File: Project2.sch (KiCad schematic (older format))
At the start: 4 parts

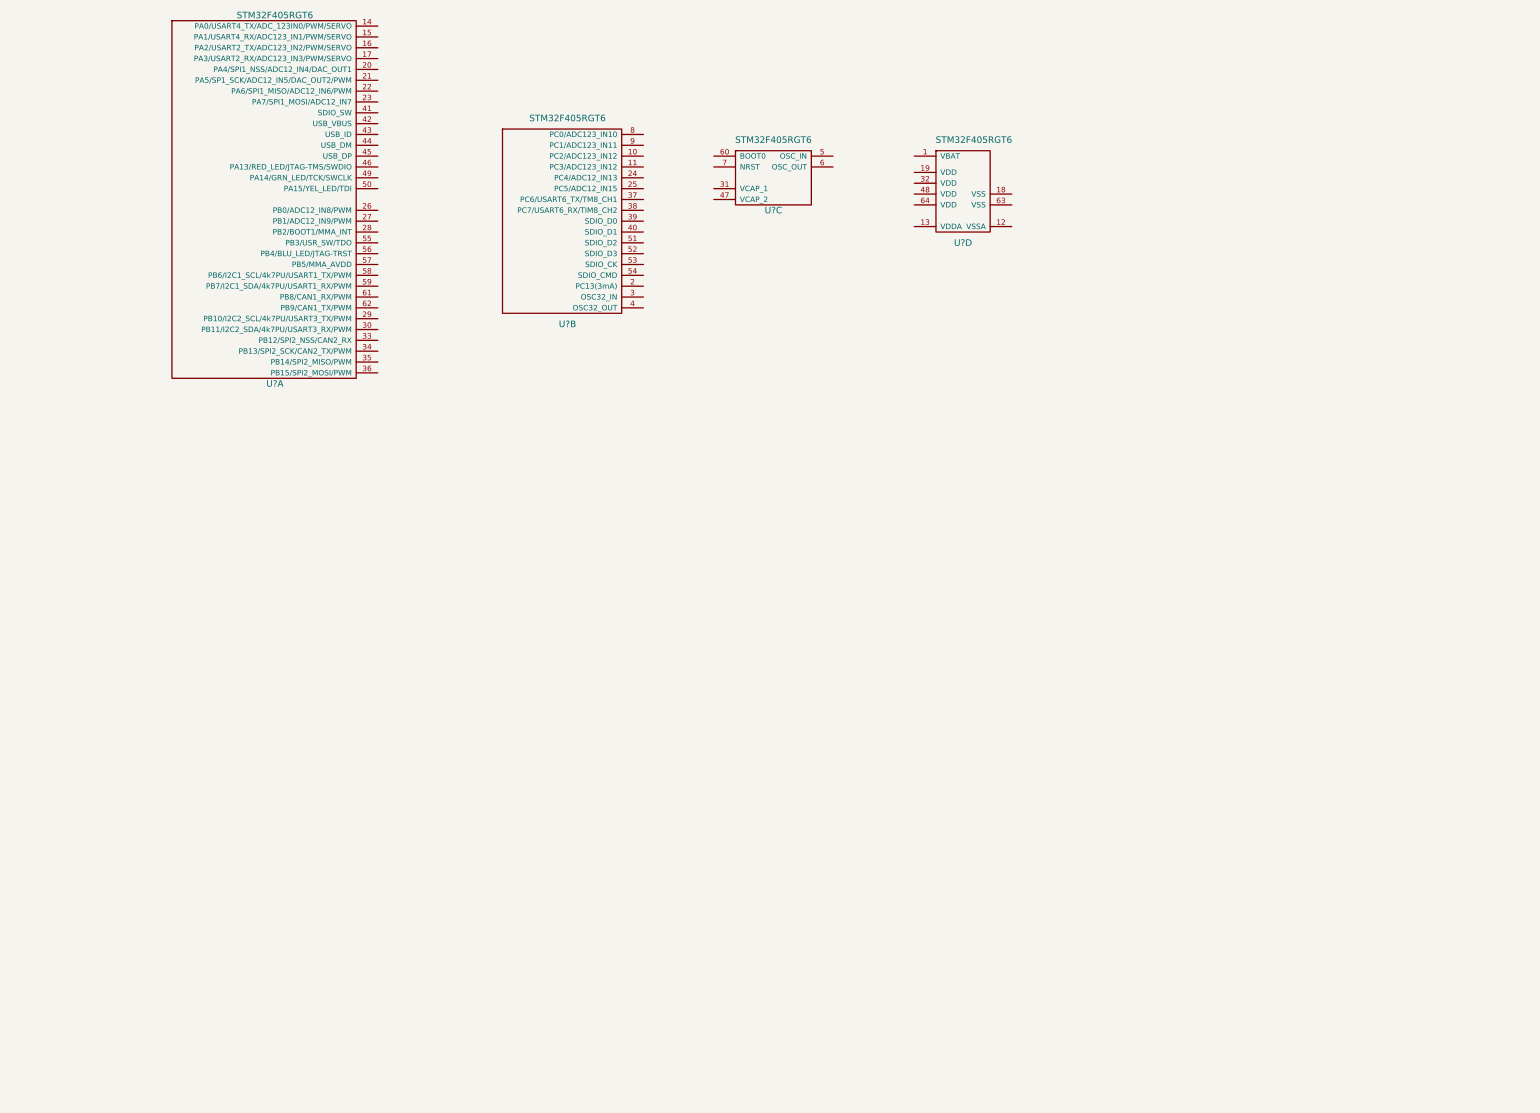
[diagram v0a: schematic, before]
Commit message: Started work on big schematic
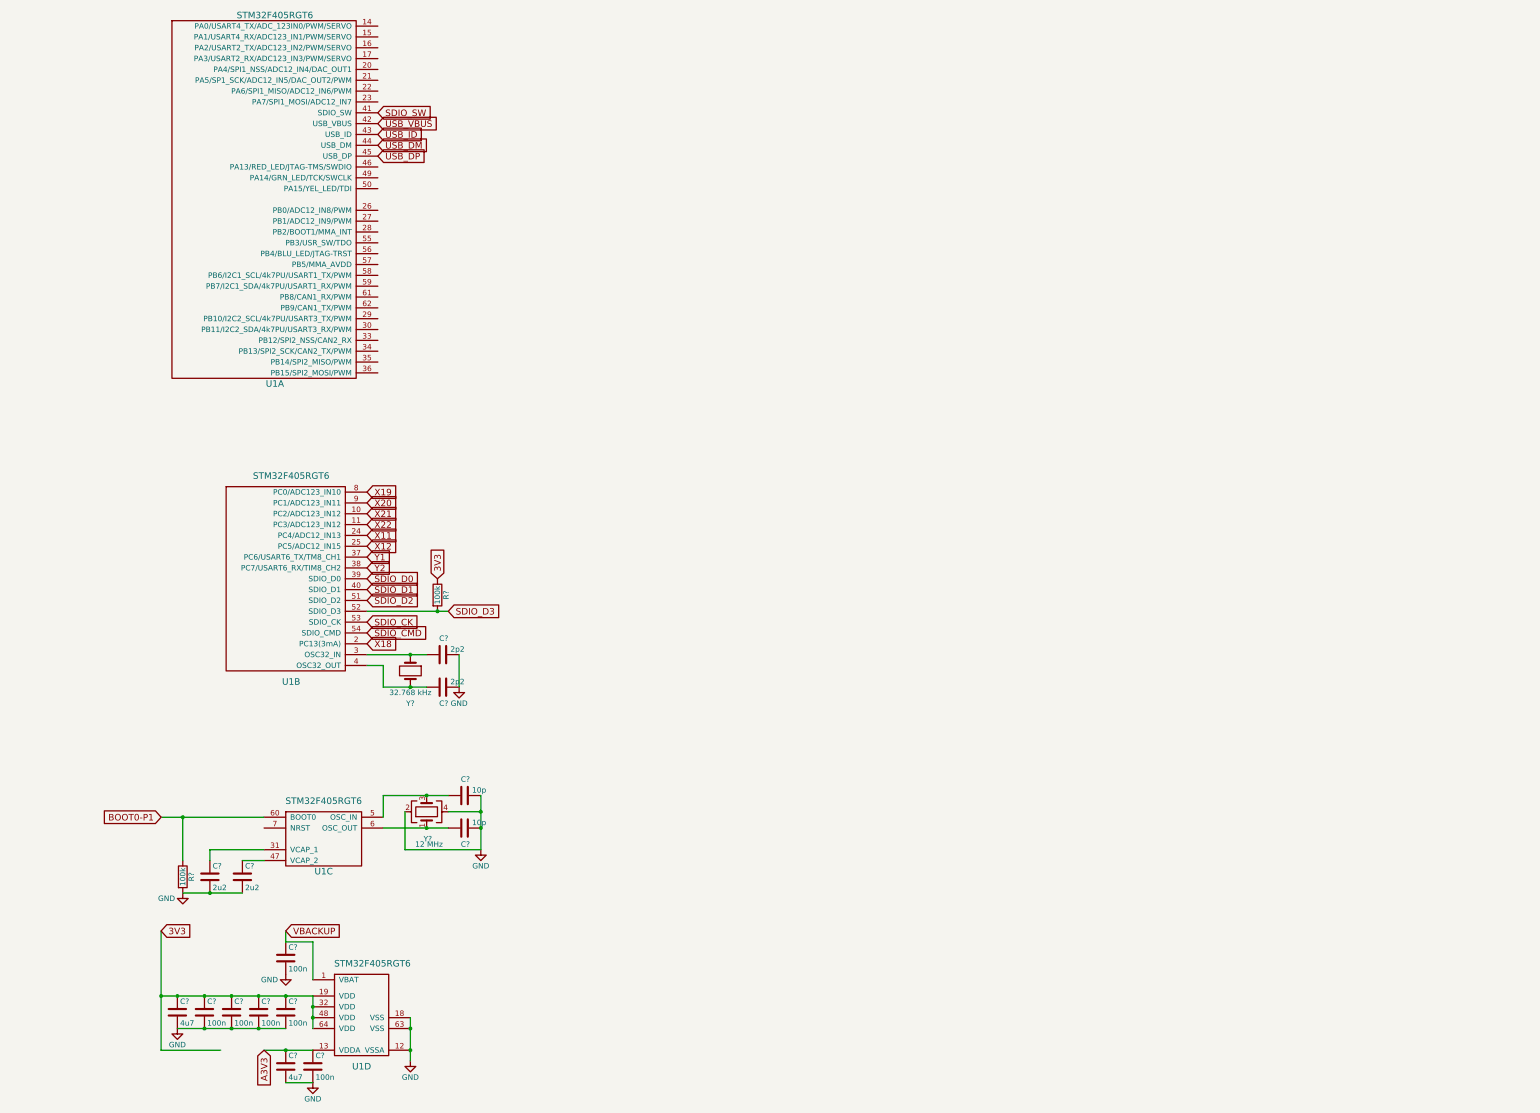
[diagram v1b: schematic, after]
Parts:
- added C? (x6): 100n, symbol C
- added C? (x2): 4u7, symbol C
- added C? (x2): 10p, symbol C
- added C? (x2): 2u2, symbol C
- added C? (x2): 2p2, symbol C
- added R? (x2): 100k, symbol R
- added Y?: 12 MHz, symbol Crystal_GND24
- added Y?: 32.768 kHz, symbol Crystal
- gave numbers to parts that had none: 1
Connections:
- net SDIO_SW: now reaches U1.41 (SDIO_SW)
- net USB_VBUS: now reaches U1.42 (USB_VBUS)
- net USB_ID: now reaches U1.43 (USB_ID)
- net USB_DM: now reaches U1.44 (USB_DM)
- net USB_DP: now reaches U1.45 (USB_DP)
- net X21: now reaches U1.10 (PC2/ADC123_IN12)
- net X22: now reaches U1.11 (PC3/ADC123_IN12)
- net X18: now reaches U1.2 (PC13(3mA))
- net X11: now reaches U1.24 (PC4/ADC12_IN13)
- net X12: now reaches U1.25 (PC5/ADC12_IN15)
- net at U1.3 (OSC32_IN): now also C?.1, Y?.1
- net Y1: now reaches U1.37 (PC6/USART6_TX/TM8_CH1)
- net Y2: now reaches U1.38 (PC7/USART6_RX/TIM8_CH2)
- net SDIO_D0: now reaches U1.39 (SDIO_D0)
- net at U1.4 (OSC32_OUT): now also C?.1, Y?.2
- net SDIO_D1: now reaches U1.40 (SDIO_D1)
- net SDIO_D2: now reaches U1.51 (SDIO_D2)
- net SDIO_D3: now reaches U1.52 (SDIO_D3)
- net SDIO_D3: now also R?.2
- net SDIO_CK: now reaches U1.53 (SDIO_CK)
- net SDIO_CMD: now reaches U1.54 (SDIO_CMD)
- net X19: now reaches U1.8 (PC0/ADC123_IN10)
- net X20: now reaches U1.9 (PC1/ADC123_IN11)
- net at U1.31 (VCAP_1): now also C?.1
- net at U1.47 (VCAP_2): now also C?.1
- net at U1.5 (OSC_IN): now also C?.1, Y?.3
- net at U1.6 (OSC_OUT): now also C?.1, Y?.1
- net BOOT0-P1: now reaches U1.60 (BOOT0)
- net BOOT0-P1: now also R?.1
- net VBACKUP: now reaches U1.1 (VBAT)
- net VBACKUP: now also C?.1
- net GND: now reaches U1.12 (VSSA)
- net GND: now also U1.18 (VSS), U1.63 (VSS), C?.2, C?.2, C?.2, C?.2, C?.2, C?.2, C?.2, C?.2, C?.2, C?.2, C?.2, C?.2, C?.2, C?.2, R?.2, Y?.2, Y?.4
- net A3V3: now reaches U1.13 (VDDA)
- net A3V3: now also C?.1, C?.1
- net 3V3: now reaches U1.19 (VDD)
- net 3V3: now also U1.32 (VDD), U1.48 (VDD), U1.64 (VDD), C?.1, C?.1, C?.1, C?.1, C?.1, R?.1
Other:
- moved on the sheet: U1B, U1C, U1D

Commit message: Finished (?) the schematic
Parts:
- added C? (x3): 100n, symbol C
- added C?: 2u2, symbol C
- added C? (x2): 4u7, symbol C
- added D?: LED_RED, symbol LED
- added D?: LED_GREEN, symbol LED
- added D?: LED_YELLOW, symbol LED
- added D?: LED_BLUE, symbol LED
- added J?: Header_8-P1P8, symbol Header_8-P1P8
- added J?: Header_8-X1X8, symbol Header_8-X1X8
- added J?: Header_8-X9X16, symbol Header_8-X9X16
- added J?: Header_8-Y1Y8, symbol Header_8-Y1Y8
- added J?: Header_8-Y9Y16, symbol Header_8-Y9Y16
- added J?: Header_P9P10, symbol Header_P9P10
- added J?: Header_X17X24, symbol Header_X17X24
- added J?: CON-USB-MICROAB, symbol CON-USB-MICROAB
- added J?: Proj2Battery, symbol Proj2Battery
- added J?: MicroSD-PUSH_PULL, symbol MicroSD-PUSH_PULL
- added L?: 1k, symbol Ferrite_Bead
- added MSE1PB-M3/89A: D, symbol D
- added Q?: DMP2160UW, symbol Q_PMOS_GSD
- added R? (x4): 110, symbol R
- added R?: 4k7, symbol R
- added R? (x5): 60.4, symbol R
- added R? (x5): 499, symbol R
- added R? (x4): 11, symbol R
- added R? (x4): 100k, symbol R
- added R? (x5): 4.75k, symbol R
- added SW? (x2): USR, symbol SW_DPST
- added U?: MMA7660FC, symbol MMA7660FC
- added U?: MIC2005A-1YM5-TR, symbol MIC2005A-1YM5-TR
- added U?: MCP1702, symbol MCP1702
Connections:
- net 3V3: now also C?.1, C?.2, C?.2, J?.4 (VDD), J?.7 (X15), J?.7 (Y15), L?.2, R?.1, R?.1, R?.1, R?.1, R?.1, R?.1, U?.2 (OUT), U?.9 (DVDD)
- net A3V3: now also J?.7 (X23), L?.1
- net GND: now also C?.1, C?.1, C?.1, C?.2, C?.2, C?.2, D?.1 (K), D?.1 (K), D?.1 (K), D?.1 (K), J?.1 (P9A), J?.2 (GND), J?.2 (P9B), J?.3 (P9C), J?.4 (P9D), J?.5 (GND), J?.6 (GDN), J?.6 (X14), J?.6 (Y14), J?.8 (P8), J?.8 (X24), J?.G1 (MOUNT), J?.G2 (MOUNT), J?.G3 (SWITCH), R?.1, R?.2, R?.2, SW?.2, SW?.2, U?.1 (RSRVD), U?.10 (RSRVD), U?.2 (GND), U?.2 (N/C), U?.4 (AVSS), U?.8 (DVSS)
- net SDIO_CK: now also J?.5 (CLK)
- net SDIO_CMD: now also J?.3 (CMD)
- net SDIO_D0: now also J?.7 (DAT0)
- net SDIO_D1: now also J?.8 (DAT1)
- net SDIO_D2: now also J?.1 (DAT2)
- net SDIO_D3: now also J?.2 (DAT3)
- net SDIO_SW: now also J?.G4 (SWITCH)
- net USB_DM: now also R?.2
- net USB_DP: now also R?.2
- net USB_ID: now also R?.2, R?.2
- net USB_VBUS: now also R?.2
- net VBACKUP: now also R?.1
- net X11: now also J?.3 (X11)
- net X12: now also J?.4 (X12)
- net X18: now also J?.2 (X18)
- net X19: now also J?.3 (X19)
- net X20: now also J?.4 (X20)
- net X21: now also J?.5 (X21)
- net X22: now also J?.6 (X22)
- net Y1: now also J?.1 (Y1)
- net Y2: now also J?.2 (Y2)
- net X1: now reaches U1.14 (PA0/USART4_TX/ADC_123IN0/PWM/SERVO)
- net X1: now also J?.1 (X1)
- net X2: now reaches U1.15 (PA1/USART4_RX/ADC123_IN1/PWM/SERVO)
- net X2: now also J?.2 (X2)
- net X3: now reaches U1.16 (PA2/USART2_TX/ADC123_IN2/PWM/SERVO)
- net X3: now also J?.3 (X3)
- net X4: now reaches U1.17 (PA3/USART2_RX/ADC123_IN3/PWM/SERVO)
- net X4: now also J?.4 (X4)
- net X5: now reaches U1.20 (PA4/SPI1_NSS/ADC12_IN4/DAC_OUT1)
- net X5: now also J?.5 (X5)
- net X6: now reaches U1.21 (PA5/SP1_SCK/ADC12_IN5/DAC_OUT2/PWM)
- net X6: now also J?.6 (X6)
- net X7: now reaches U1.22 (PA6/SPI1_MISO/ADC12_IN6/PWM)
- net X7: now also J?.7 (X7)
- net X8: now reaches U1.23 (PA7/SPI1_MOSI/ADC12_IN7)
- net X8: now also J?.8 (X8)
- net Y11: now reaches U1.26 (PB0/ADC12_IN8/PWM)
- net Y11: now also J?.3 (Y11)
- net Y12: now reaches U1.27 (PB1/ADC12_IN9/PWM)
- net Y12: now also J?.4 (Y12)
- net BOOT1_MMA_INT: now reaches U1.28 (PB2/BOOT1/MMA_INT)
- net BOOT1_MMA_INT: now also R?.1, U?.5 (INT)
- net Y9: now reaches U1.29 (PB10/I2C2_SCL/4k7PU/USART3_TX/PWM)
- net Y9: now also J?.1 (Y9), R?.2
- net Y10: now reaches U1.30 (PB11/I2C2_SDA/4k7PU/USART3_RX/PWM)
- net Y10: now also J?.2 (Y10), R?.2
- net Y5: now reaches U1.33 (PB12/SPI2_NSS/CAN2_RX)
- net Y5: now also J?.5 (Y5)
- net Y6: now reaches U1.34 (PB13/SPI2_SCK/CAN2_TX/PWM)
- net Y6: now also J?.6 (Y6)
- net Y7: now reaches U1.35 (PB14/SPI2_MISO/PWM)
- net Y7: now also J?.7 (Y7)
- net Y8: now reaches U1.36 (PB15/SPI2_MOSI/PWM)
- net Y8: now also J?.8 (Y8)
- net RED_P5: now reaches U1.46 (PA13/RED_LED/JTAG-TMS/SWDIO)
- net RED_P5: now also J?.5 (P5), R?.2
- net GRN_P4: now reaches U1.49 (PA14/GRN_LED/TCK/SWCLK)
- net GRN_P4: now also J?.4 (P4), R?.2
- net YEL_P3: now reaches U1.50 (PA15/YEL_LED/TDI)
- net YEL_P3: now also J?.3 (P3), R?.2
- net SW_X17: now reaches U1.55 (PB3/USR_SW/TDO)
- net SW_X17: now also J?.1 (X17), R?.1
- net BLU_P2: now reaches U1.56 (PB4/BLU_LED/JTAG-TRST)
- net BLU_P2: now also J?.2 (P2), R?.2
- net MMA_AVDD: now reaches U1.57 (PB5/MMA_AVDD)
- net MMA_AVDD: now also C?.2, R?.1, U?.3 (AVDD)
- net SCL_X9: now reaches U1.58 (PB6/I2C1_SCL/4k7PU/USART1_TX/PWM)
- net SCL_X9: now also J?.1 (X9), R?.2
- net SDA_X10: now reaches U1.59 (PB7/I2C1_SDA/4k7PU/USART1_RX/PWM)
- net SDA_X10: now also J?.2 (X10), R?.2
- net Y3: now reaches U1.61 (PB8/CAN1_RX/PWM)
- net Y3: now also J?.3 (Y3)
- net Y4: now reaches U1.62 (PB9/CAN1_TX/PWM)
- net Y4: now also J?.4 (Y4)
- net RST#: now reaches U1.7 (NRST)
- net RST#: now also C?.1, J?.5 (X13), J?.5 (Y13), R?.2, SW?.1
- new net: J?.6 (P6), R?.2
- new net: R?.1, R?.2 (x9)
- new net: R?.2, SW?.1
- new net: D?.2 (A), R?.1 (x4)
- new net: J?.1 (VBUS), MSE1PB-M3/89A.2 (A), Q?.1 (G), R?.1, R?.2, U?.5 (OUT)
- new net: J?.2 (DM), R?.1
- new net: J?.3 (DP), R?.1
- new net: J?.4 (ID), R?.1
- new net: J?.1 (PWR), Q?.3 (D)
- new net B: U?.3 (EN)
- new net BOOT0_P1: J?.1 (P1)
- new net V+: C?.1, J?.5 (P10A), J?.6 (P10B), J?.7 (P10C), J?.7 (P7), J?.8 (P10D), J?.8 (X16), J?.8 (Y16), MSE1PB-M3/89A.1 (K), Q?.2 (S), U?.1 (IN), U?.3 (IN)
- no-connect marks 0 -> 5

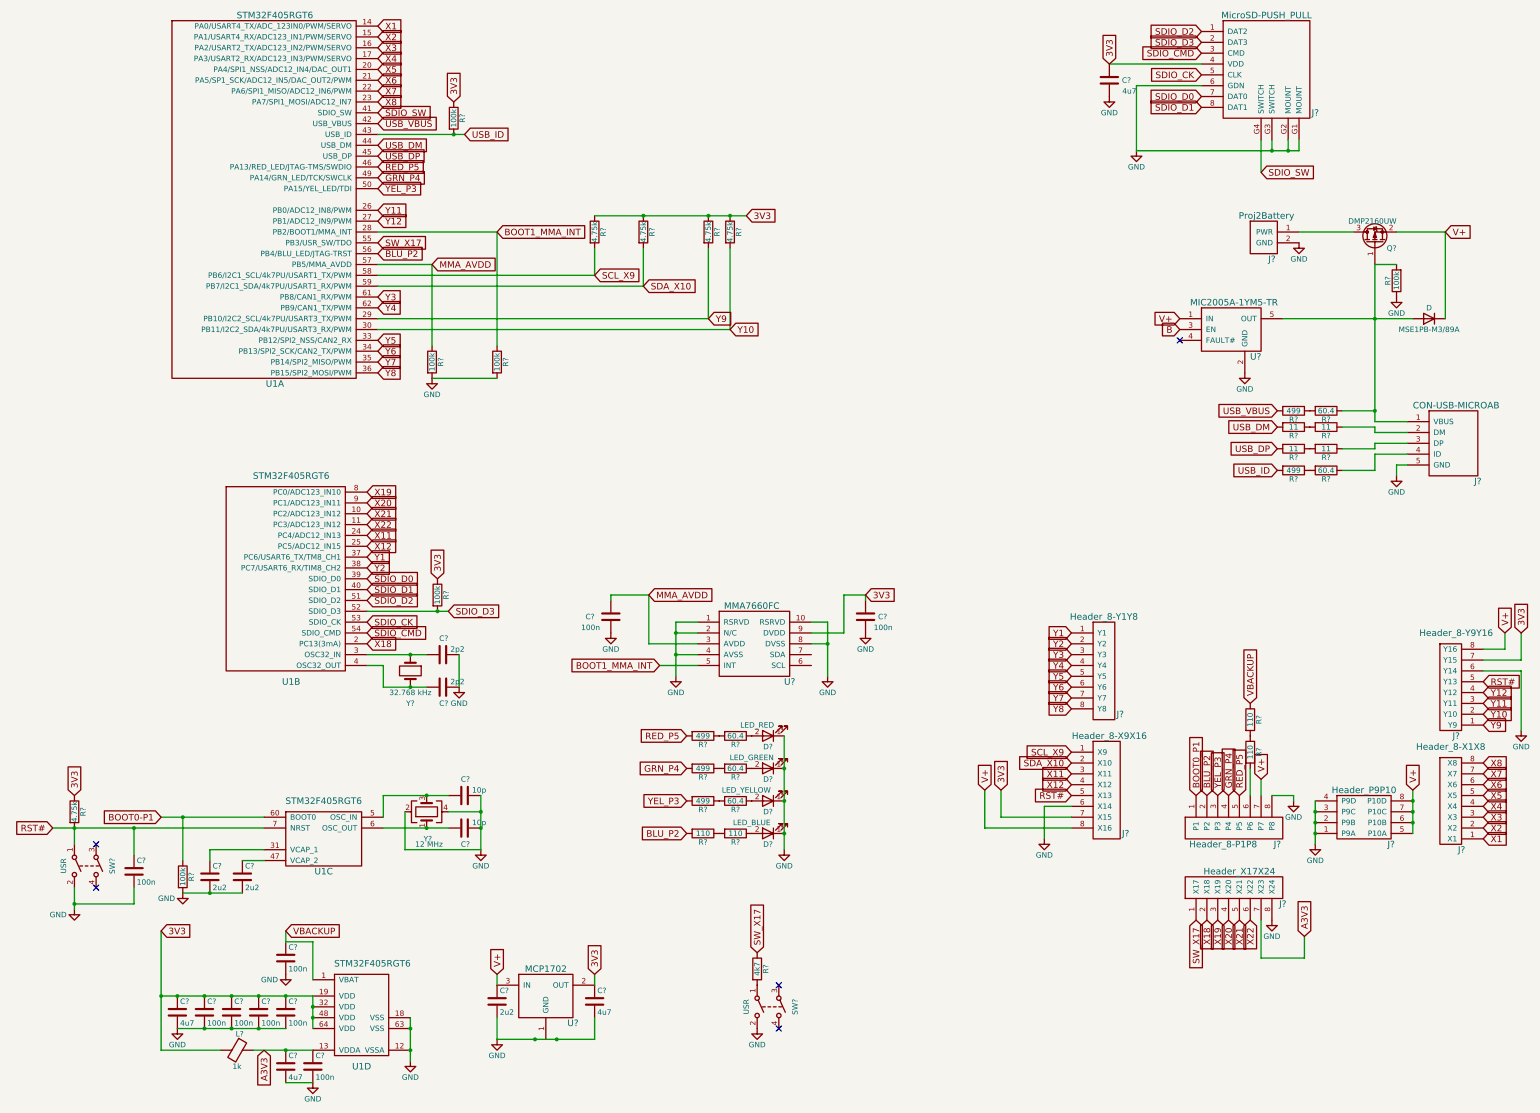
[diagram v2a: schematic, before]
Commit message: A couple schematic changes, footprint library, and microcontroller footprint
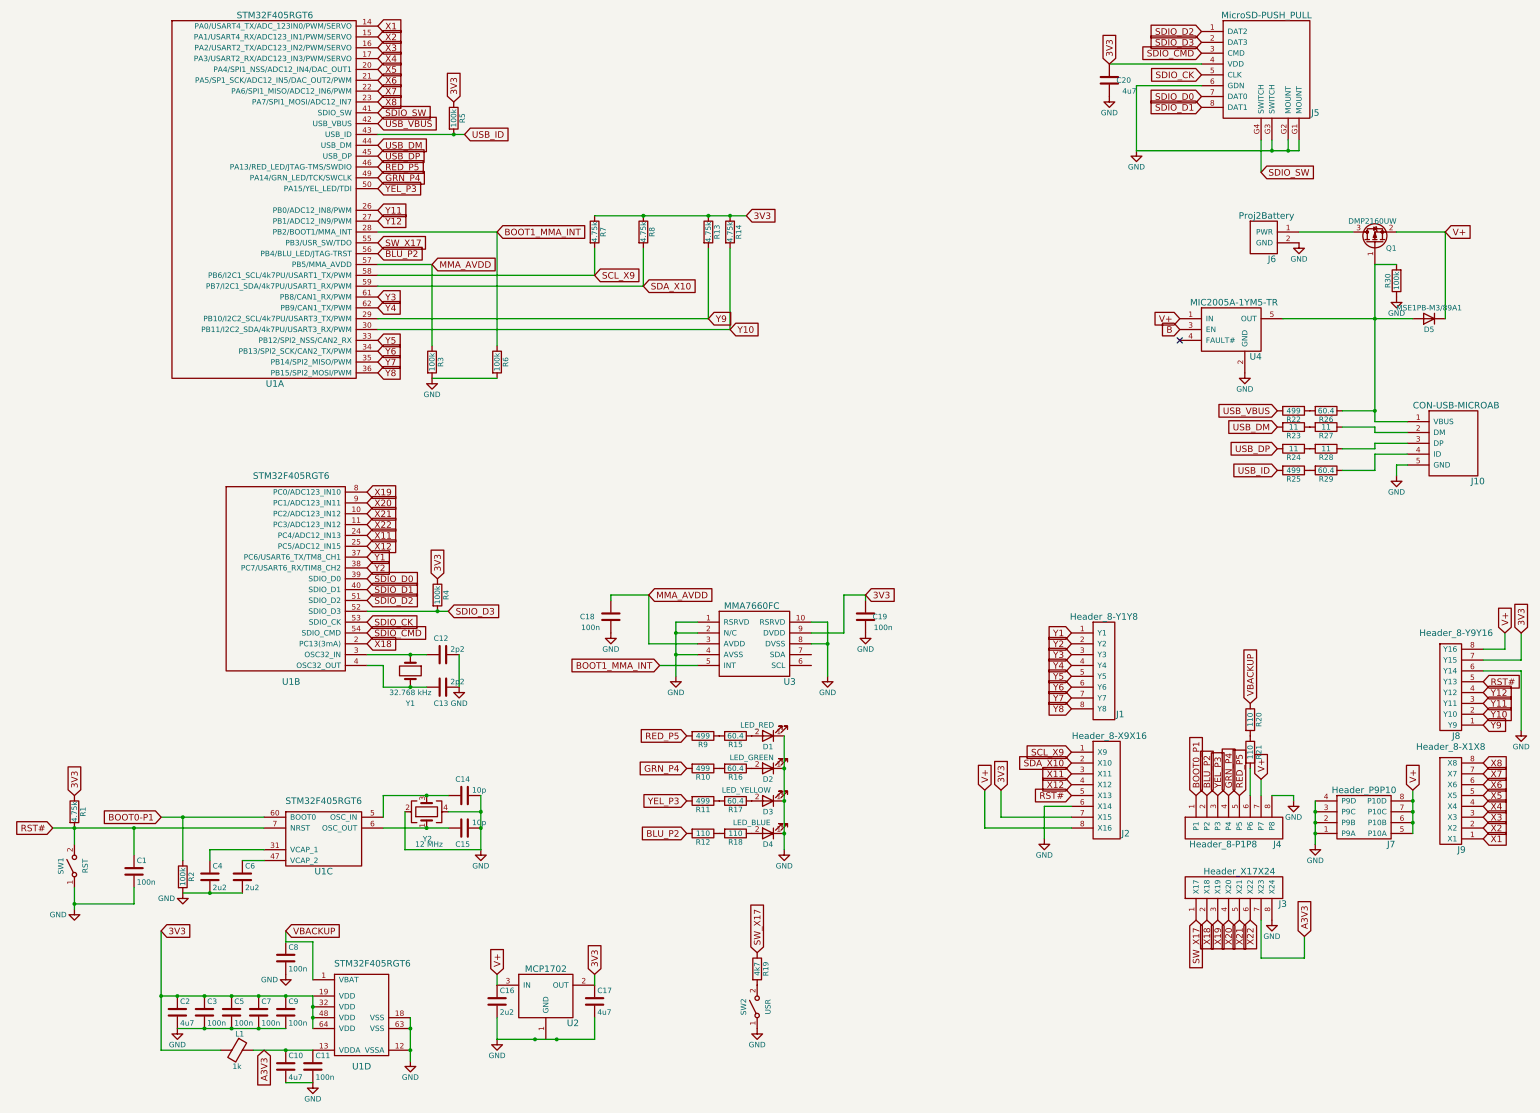
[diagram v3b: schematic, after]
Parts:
- removed SW? (x2): USR, symbol SW_DPST
- added SW1: RST, symbol SW_SPST
- added SW2: USR, symbol SW_SPST
- C1, C10, C11, C12, C13, C14, C15, C16, C17, C18, C19, C2, C20, C3, C4, C5, C6, C7, C8, C9: renamed from C?; footprint (none) -> Capacitors_SMD:C_0603
- D1, D2, D3, D4: renamed from D?; footprint (none) -> LEDs:LED_0805
- D5: renamed from MSE1PB-M3/89A; value D -> MSE1PB-M3/89A1
- L1: renamed from L?; footprint (none) -> Inductors_SMD:L_0603
- R1, R10, R11, R12, R13, R14, R15, R16, R17, R18, R19, R2, R20, R21, R22, R23, R24, R25, R26, R27, R28, R29, R3, R30, R4, R5, R6, R7, R8, R9: renamed from R?; footprint (none) -> Resistors_SMD:R_0603
- U4: renamed from U?; footprint (none) -> TO_SOT_Packages_SMD:SOT-23-5
- Y1: renamed from Y?; footprint (none) -> Crystals:Crystal_SMD_3215-2pin_3.2x1.5mm
- Y2: renamed from Y?; footprint (none) -> Crystals:Crystal_SMD_3225-4pin_3.2x2.5mm
- gave numbers to parts that had none: 13
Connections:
- net GND: now also SW1.1 (A), SW2.1 (A)
- net RST#: now also SW1.2 (B)
- net at R19.2: now also SW2.2 (B)
- no-connect marks 5 -> 1
